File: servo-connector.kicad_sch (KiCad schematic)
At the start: 35 parts, among them J2 SERVO_SIG, J3 SERVO_SIG, J4 SERVO_SIG, J5 SERVO_SIG, J6 SERVO_SIG, J7 SERVO_SIG, J8 SERVO_SIG

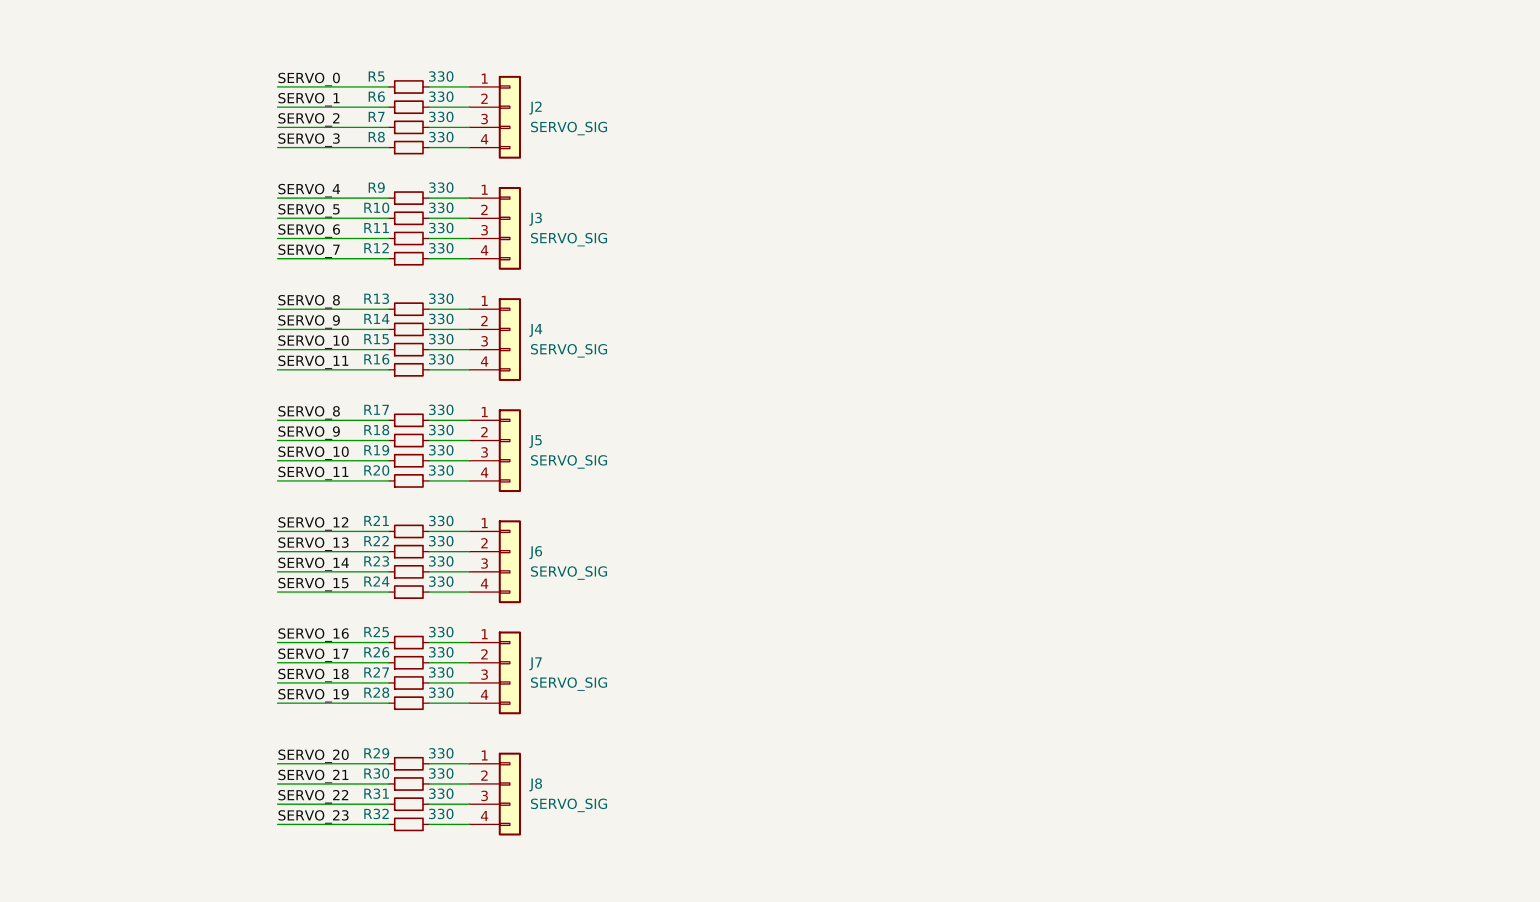
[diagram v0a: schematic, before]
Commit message: Added servo-connector, BNO055, power (not finished)
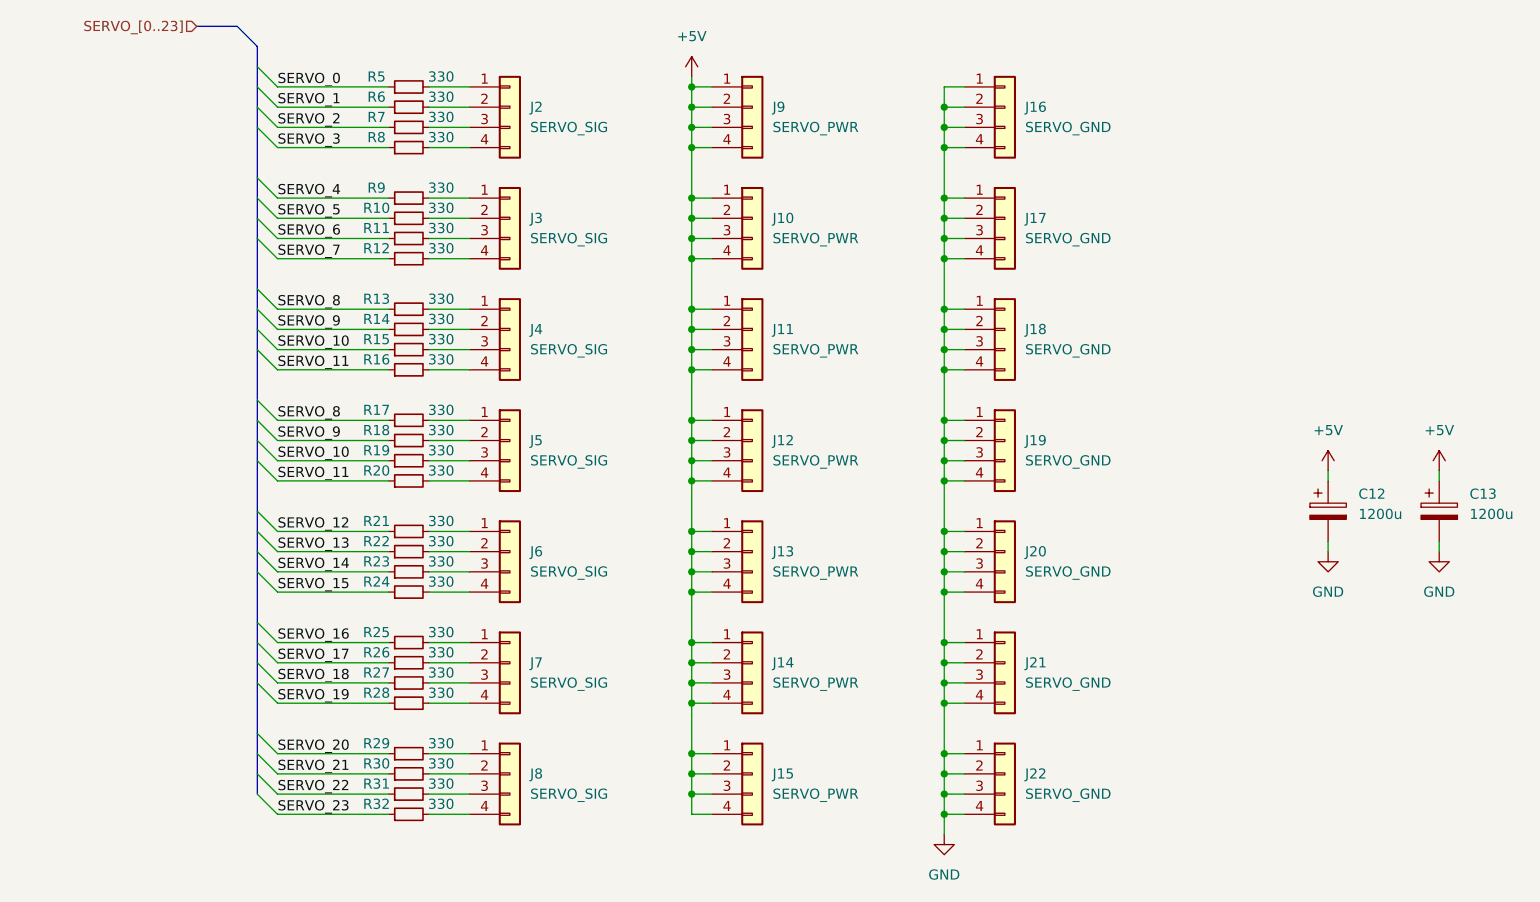
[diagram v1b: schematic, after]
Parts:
- added C12, C13: 1200u, symbol Device:C_Polarized
- added J10, J11, J12, J13, J14, J15, J9: SERVO_PWR, symbol Connector_Generic:Conn_01x04
- added J16, J17, J18, J19, J20, J21, J22: SERVO_GND, symbol Connector_Generic:Conn_01x04
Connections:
- new net +5V: C12.1, C13.1, J10.1 (Pin_1), J10.2 (Pin_2), J10.3 (Pin_3), J10.4 (Pin_4), J11.1 (Pin_1), J11.2 (Pin_2), J11.3 (Pin_3), J11.4 (Pin_4), J12.1 (Pin_1), J12.2 (Pin_2), J12.3 (Pin_3), J12.4 (Pin_4), J13.1 (Pin_1), J13.2 (Pin_2), J13.3 (Pin_3), J13.4 (Pin_4), J14.1 (Pin_1), J14.2 (Pin_2), J14.3 (Pin_3), J14.4 (Pin_4), J15.1 (Pin_1), J15.2 (Pin_2), J15.3 (Pin_3), J15.4 (Pin_4), J9.1 (Pin_1), J9.2 (Pin_2), J9.3 (Pin_3), J9.4 (Pin_4)
- new net GND: C12.2, C13.2, J16.1 (Pin_1), J16.2 (Pin_2), J16.3 (Pin_3), J16.4 (Pin_4), J17.1 (Pin_1), J17.2 (Pin_2), J17.3 (Pin_3), J17.4 (Pin_4), J18.1 (Pin_1), J18.2 (Pin_2), J18.3 (Pin_3), J18.4 (Pin_4), J19.1 (Pin_1), J19.2 (Pin_2), J19.3 (Pin_3), J19.4 (Pin_4), J20.1 (Pin_1), J20.2 (Pin_2), J20.3 (Pin_3), J20.4 (Pin_4), J21.1 (Pin_1), J21.2 (Pin_2), J21.3 (Pin_3), J21.4 (Pin_4), J22.1 (Pin_1), J22.2 (Pin_2), J22.3 (Pin_3), J22.4 (Pin_4)
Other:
- moved on the sheet: J8, R29, R30, R31, R32

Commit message: Add zener to each servo pin, add I2C and UART connector
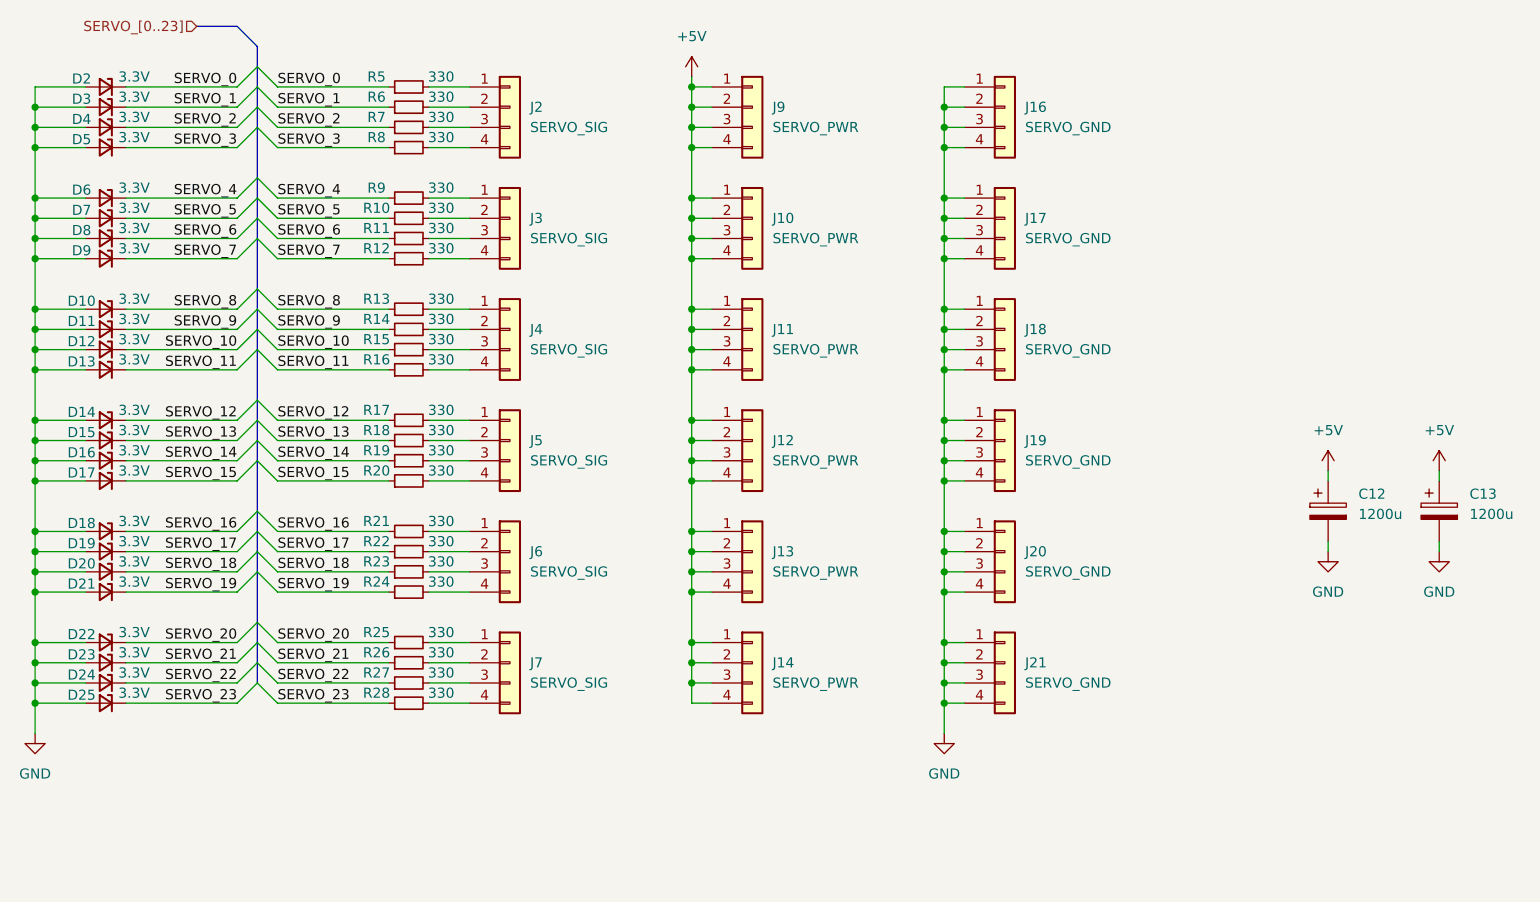
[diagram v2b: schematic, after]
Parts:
- removed J15: SERVO_PWR, symbol Connector_Generic:Conn_01x04
- removed J22: SERVO_GND, symbol Connector_Generic:Conn_01x04
- removed J8: SERVO_SIG, symbol Connector_Generic:Conn_01x04
- removed R29, R30, R31, R32: 330, symbol Device:R_Small
- added D10, D11, D12, D13, D14, D15, D16, D17, D18, D19, D2, D20, D21, D22, D23, D24, D25, D3, D4, D5, D6, D7, D8, D9: 3.3V, Diode_SMD:D_SOD-523, symbol Device:D_Zener_Small
- C12, C13: footprint (none) -> Capacitor_THT:CP_Radial_D10.0mm_P5.00mm
- J10, J11, J12, J13, J14, J16, J17, J18, J19, J2, J20, J21, J3, J4, J5, J6, J7, J9: footprint (none) -> Connector_PinHeader_2.54mm:PinHeader_1x04_P2.54mm_Vertical
- R10, R11, R12, R13, R14, R15, R16, R17, R18, R19, R20, R21, R22, R23, R24, R25, R26, R27, R28, R5, R6, R7, R8, R9: footprint (none) -> Resistor_SMD:R_0402_1005Metric
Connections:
- net GND: now also D10.2 (A), D11.2 (A), D12.2 (A), D13.2 (A), D14.2 (A), D15.2 (A), D16.2 (A), D17.2 (A), D18.2 (A), D19.2 (A), D2.2 (A), D20.2 (A), D21.2 (A), D22.2 (A), D23.2 (A), D24.2 (A), D25.2 (A), D3.2 (A), D4.2 (A), D5.2 (A), D6.2 (A), D7.2 (A), D8.2 (A), D9.2 (A)
- net SERVO_0: now also D2.1 (K)
- net SERVO_1: now also D3.1 (K)
- net SERVO_10: now also D12.1 (K); no longer R19.1
- net SERVO_11: now also D13.1 (K); no longer R20.1
- net SERVO_12: now also R17.1, D14.1 (K); no longer R21.1
- net SERVO_13: now also R18.1, D15.1 (K); no longer R22.1
- net SERVO_14: now also R19.1, D16.1 (K); no longer R23.1
- net SERVO_15: now also R20.1, D17.1 (K); no longer R24.1
- net SERVO_16: now also R21.1, D18.1 (K); no longer R25.1
- net SERVO_17: now also R22.1, D19.1 (K); no longer R26.1
- net SERVO_18: now also R23.1, D20.1 (K); no longer R27.1
- net SERVO_19: now also R24.1, D21.1 (K); no longer R28.1
- net SERVO_2: now also D4.1 (K)
- net SERVO_20: now also R25.1, D22.1 (K)
- net SERVO_21: now also R26.1, D23.1 (K)
- net SERVO_22: now also R27.1, D24.1 (K)
- net SERVO_23: now also R28.1, D25.1 (K)
- net SERVO_3: now also D5.1 (K)
- net SERVO_4: now also D6.1 (K)
- net SERVO_5: now also D7.1 (K)
- net SERVO_6: now also D8.1 (K)
- net SERVO_7: now also D9.1 (K)
- net SERVO_8: now also D10.1 (K); no longer R17.1
- net SERVO_9: now also D11.1 (K); no longer R18.1
